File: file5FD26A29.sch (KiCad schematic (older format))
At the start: 4 parts

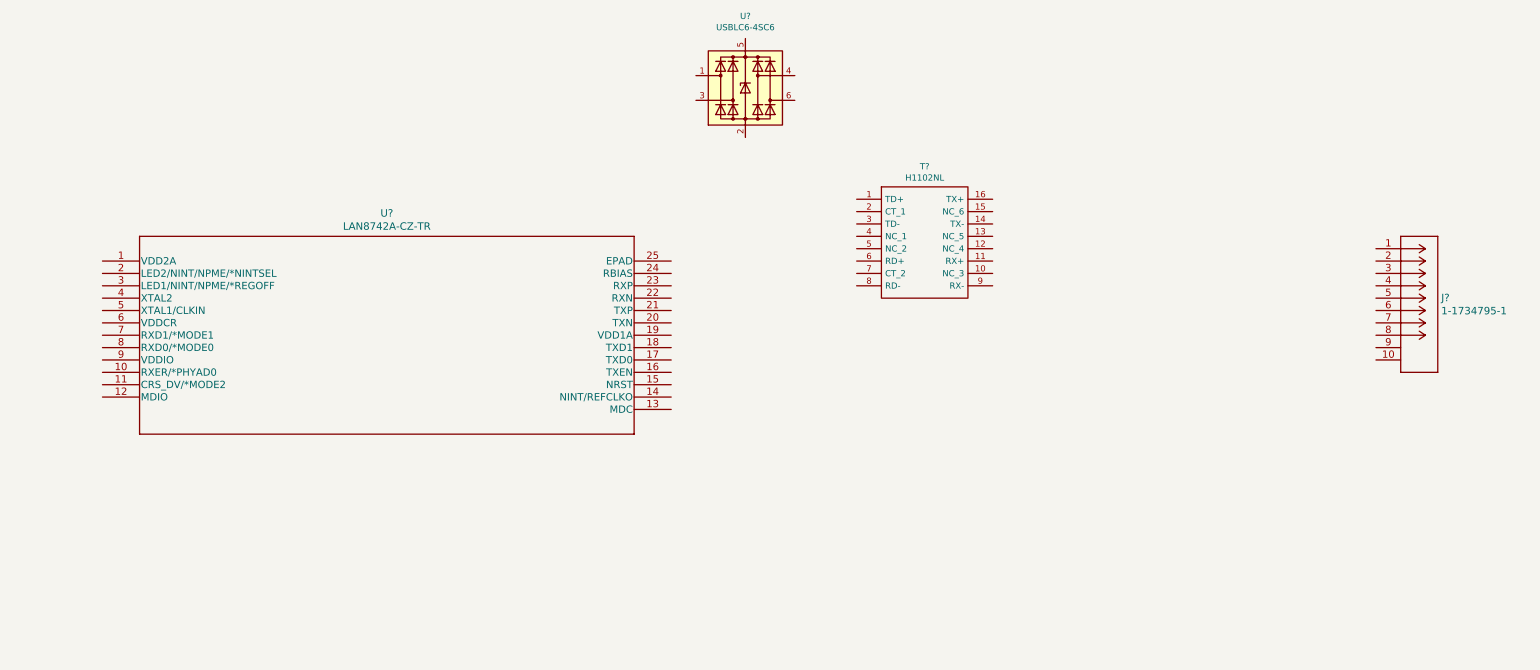
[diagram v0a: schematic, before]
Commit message: Change Ethernet jack
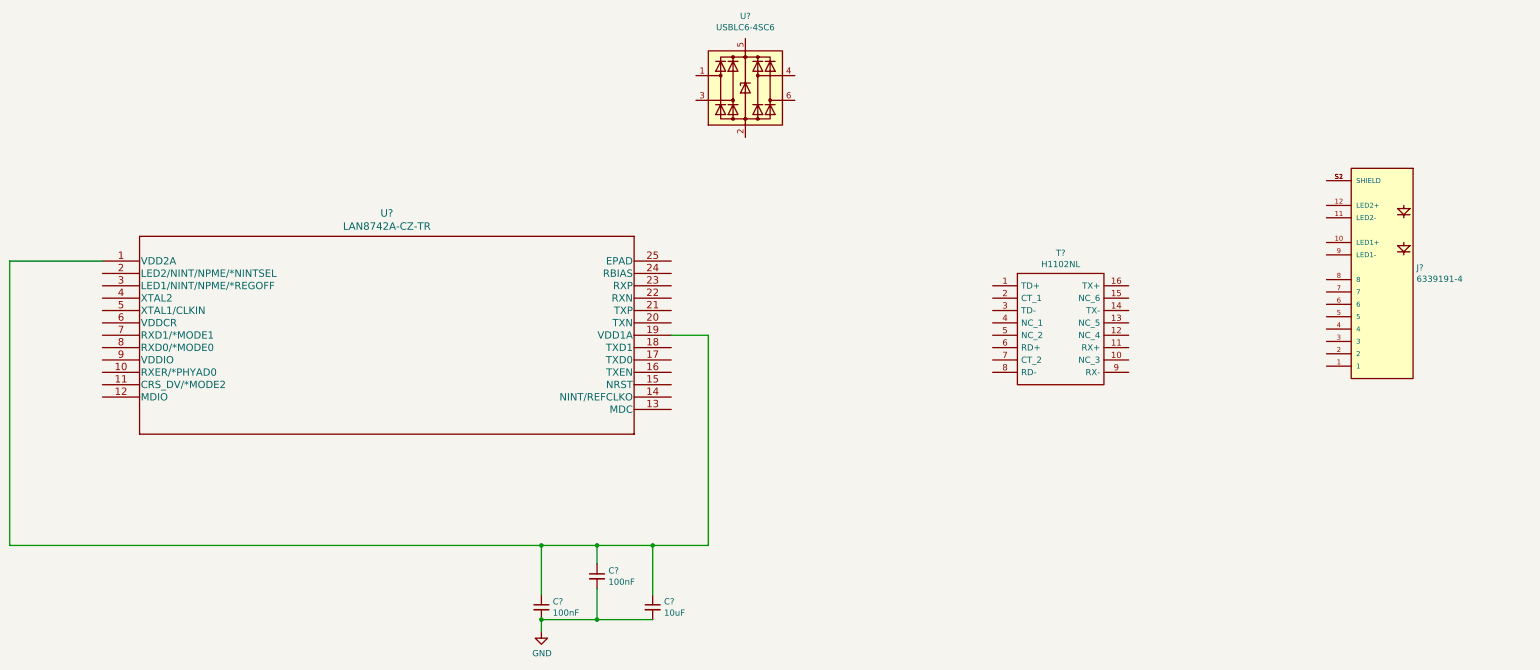
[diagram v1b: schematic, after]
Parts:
- removed J?: 1-1734795-1, CONN12_1-1734795-1_TEC, symbol 2020-12-10_19-10-13:1-1734795-1
- added C? (x2): 100nF, symbol Device:C_Small
- added C?: 10uF, symbol Device:C_Small
- added J?: 6339191-4, TE_6339191-4, symbol 6339191-4:6339191-4
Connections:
- net at U?.1 (VDD2A): now also U?.19 (VDD1A), C?.1, C?.1, C?.1
- new net: J?.S1 (SHIELD), J?.S2 (SHIELD)
- new net GND: C?.2, C?.2, C?.2
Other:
- moved on the sheet: T?
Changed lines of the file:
@@
 L H1102NL:H1102NL T?
 U 1 1 5FD29DFA
-P 8750 4550
-F 0 "T?" H 9300 4815 50  0000 C CNN
-F 1 "H1102NL" H 9300 4724 50  0000 C CNN
-F 2 "SOIC127P940X597-16N" H 9700 4650 50  0001 L CNN
-F 3 "https://productfinder.pulseeng.com/products/datasheets/h1102nl.pdf" H 9700 4550 50  0001 L CNN
-F 4 "PULSE ELECTRONICS - H1102NL - TRANSFORMER, 1:1, 1PORT, 100BASE-TX, SMT" H 9700 4450 50  0001 L CNN "Description"
-F 5 "5.97" H 9700 4350 50  0001 L CNN "Height"
-F 6 "Pulse" H 9700 4250 50  0001 L CNN "Manufacturer_Name"
-F 7 "H1102NL" H 9700 4150 50  0001 L CNN "Manufacturer_Part_Number"
-F 8 "H1102NL" H 9700 4050 50  0001 L CNN "Arrow Part Number"
-F 9 "https://www.arrow.com/en/products/h1102nl/pulse-electronics-corporation" H 9700 3950 50  0001 L CNN "Arrow Price/Stock"
-F 10 "673-H1102NL" H 9700 3850 50  0001 L CNN "Mouser Part Number"
-F 11 "https://www.mouser.co.uk/ProductDetail/Pulse-Electronics/H1102NL?qs=EKu32SdDin%2FHU33L94JZxw%3D%3D" H 9700 3750 50  0001 L CNN "Mouser Price/Stock"
-	1    8750 4550
+P 9850 5250
+F 0 "T?" H 10400 5515 50  0000 C CNN
+F 1 "H1102NL" H 10400 5424 50  0000 C CNN
+F 2 "SOIC127P940X597-16N" H 10800 5350 50  0001 L CNN
+F 3 "https://productfinder.pulseeng.com/products/datasheets/h1102nl.pdf" H 10800 5250 50  0001 L CNN
+F 4 "PULSE ELECTRONICS - H1102NL - TRANSFORMER, 1:1, 1PORT, 100BASE-TX, SMT" H 10800 5150 50  0001 L CNN "Description"
+F 5 "5.97" H 10800 5050 50  0001 L CNN "Height"
+F 6 "Pulse" H 10800 4950 50  0001 L CNN "Manufacturer_Name"
+F 7 "H1102NL" H 10800 4850 50  0001 L CNN "Manufacturer_Part_Number"
+F 8 "H1102NL" H 10800 4750 50  0001 L CNN "Arrow Part Number"
+F 9 "https://www.arrow.com/en/products/h1102nl/pulse-electronics-corporation" H 10800 4650 50  0001 L CNN "Arrow Price/Stock"
+F 10 "673-H1102NL" H 10800 4550 50  0001 L CNN "Mouser Part Number"
+F 11 "https://www.mouser.co.uk/ProductDetail/Pulse-Electronics/H1102NL?qs=EKu32SdDin%2FHU33L94JZxw%3D%3D" H 10800 4450 50  0001 L CNN "Mouser Price/Stock"
+	1    9850 5250
 	1    0    0    -1
 $EndComp
 $Comp
-L 2020-12-10_19-10-13:1-1734795-1 J?
-U 1 1 5FD30F50
-P 12950 4950
-F 0 "J?" H 13478 4553 60  0000 L CNN
-F 1 "1-1734795-1" H 13478 4447 60  0000 L CNN
-F 2 "CONN12_1-1734795-1_TEC" H 13350 4090 60  0001 C CNN
-F 3 "" H 12950 4950 60  0000 C CNN
-	1    12950 4950
+L Device:C_Small C?
+U 1 1 5FD32DB4
+P 6200 7850
+F 0 "C?" H 6292 7896 50  0000 L CNN
+F 1 "100nF" H 6292 7805 50  0000 L CNN
+F 2 "" H 6200 7850 50  0001 C CNN
+F 3 "~" H 6200 7850 50  0001 C CNN
+	1    6200 7850
 	1    0    0    -1
 $EndComp
+$Comp
+L Device:C_Small C?
+U 1 1 5FD339FE
+P 6650 7600
+F 0 "C?" H 6742 7646 50  0000 L CNN
+F 1 "100nF" H 6742 7555 50  0000 L CNN
+F 2 "" H 6650 7600 50  0001 C CNN
+F 3 "~" H 6650 7600 50  0001 C CNN
+	1    6650 7600
+	1    0    0    -1
+$EndComp
+$Comp
+L Device:C_Small C?
+U 1 1 5FD33C45
+P 7100 7850
+F 0 "C?" H 7192 7896 50  0000 L CNN
+F 1 "10uF" H 7192 7805 50  0000 L CNN
+F 2 "" H 7100 7850 50  0001 C CNN
+F 3 "~" H 7100 7850 50  0001 C CNN
+	1    7100 7850
+	1    0    0    -1
+$EndComp
+Wire Wire Line
+	7250 5650 7550 5650
+Wire Wire Line
+	7550 5650 7550 7350
+Wire Wire Line
+	7550 7350 7100 7350
+Wire Wire Line
+	6200 7750 6200 7350
+Wire Wire Line
+	6650 7500 6650 7350
+Connection ~ 6650 7350
+Wire Wire Line
+	6650 7350 6200 7350
+Wire Wire Line
+	7100 7750 7100 7350
+Connection ~ 7100 7350
+Wire Wire Line
+	7100 7350 6650 7350
+Wire Wire Line
+	2650 5050 1900 5050
+Wire Wire Line
+	1900 5050 1900 7350
+Wire Wire Line
+	6200 7350 1900 7350
+Connection ~ 6200 7350
+Wire Wire Line
+	7100 7950 6650 7950
+Wire Wire Line
+	6650 7700 6650 7950
+Connection ~ 6650 7950
+Wire Wire Line
+	6650 7950 6200 7950
+$Comp
+L power:GND #PWR?
+U 1 1 5FD36E57
+P 6200 8050
+F 0 "#PWR?" H 6200 7800 50  0001 C CNN
+F 1 "GND" H 6205 7877 50  0000 C CNN
+F 2 "" H 6200 8050 50  0001 C CNN
+F 3 "" H 6200 8050 50  0001 C CNN
+	1    6200 8050
+	1    0    0    -1
+$EndComp
+Wire Wire Line
+	6200 8050 6200 7950
+Connection ~ 6200 7950
+$Comp
+L 6339191-4:6339191-4 J?
+U 1 1 5FD3947F
+P 13050 5200
+F 0 "J?" H 12822 5104 50  0000 R CNN
+F 1 "6339191-4" H 12822 5195 50  0000 R CNN
+F 2 "TE_6339191-4" H 13050 5200 50  0001 L BNN
+F 3 "" H 13050 5200 50  0001 L BNN
+F 4 "E3" H 13050 5200 50  0001 L BNN "PARTREV"
+F 5 "TE Connectivity" H 13050 5200 50  0001 L BNN "MANUFACTURER"
+F 6 "Manufacturer Recommendation" H 13050 5200 50  0001 L BNN "STANDARD"
+	1    13050 5200
+	-1   0    0    1
+$EndComp
 $EndSCHEMATC

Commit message: Change PS to SMPS 5v, LDO 3.3V
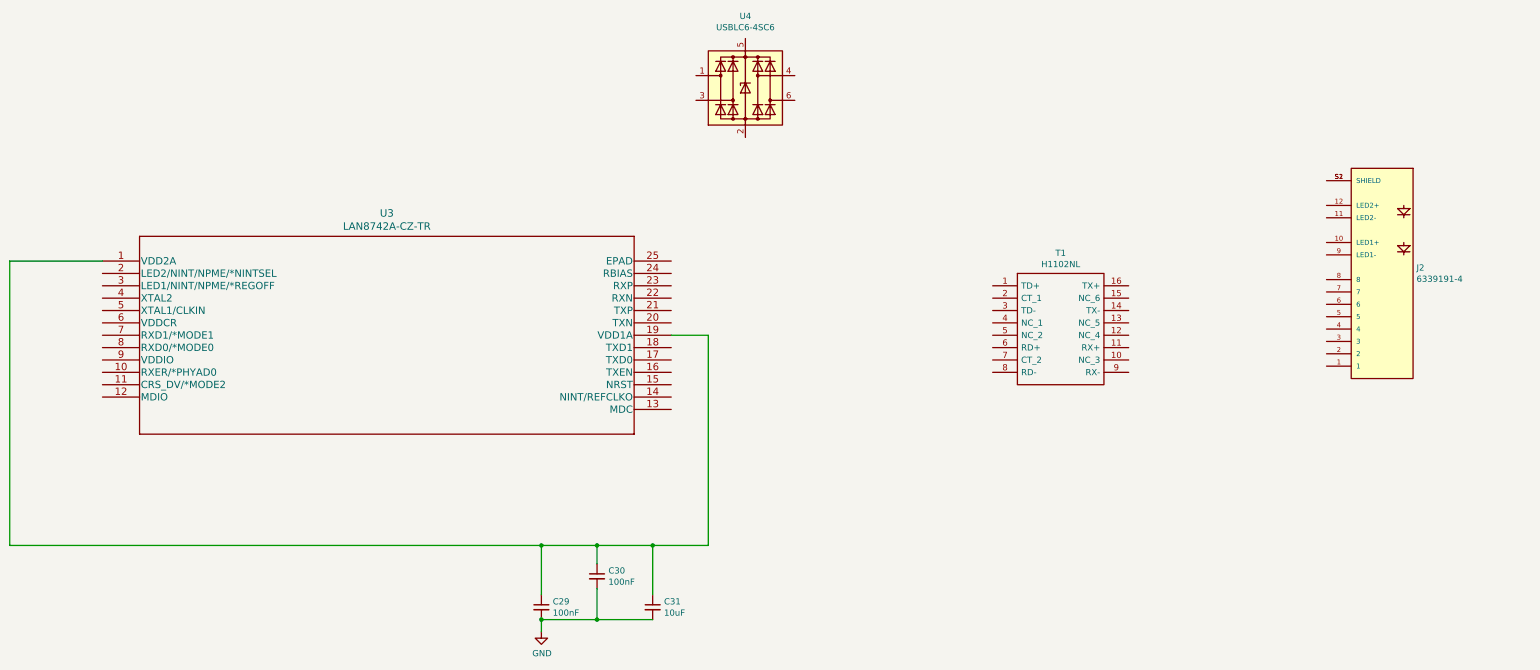
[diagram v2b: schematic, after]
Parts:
- gave numbers to parts that had none: 7
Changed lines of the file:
@@
 $Descr USLedger 17000 11000
 encoding utf-8
-Sheet 5 5
+Sheet 5 6
 Title "KQ9P Power Controller 12VDC"
 Date "2020-12-08"
@@
 $EndDescr
 $Comp
-L 2020-12-10_18-38-26:LAN8742A-CZ-TR U?
+L 2020-12-10_18-38-26:LAN8742A-CZ-TR U3
 U 1 1 5FD274C1
 P 2650 5050
-F 0 "U?" H 4950 5437 60  0000 C CNN
+F 0 "U3" H 4950 5437 60  0000 C CNN
 F 1 "LAN8742A-CZ-TR" H 4950 5331 60  0000 C CNN
 F 2 "SQFN24_4X4MC_MCH" H 4950 5290 60  0001 C CNN
@@
 $EndComp
 $Comp
-L Power_Protection:USBLC6-4SC6 U?
+L Power_Protection:USBLC6-4SC6 U4
 U 1 1 5FD2935E
 P 7850 3650
-F 0 "U?" H 7850 4231 50  0000 C CNN
+F 0 "U4" H 7850 4231 50  0000 C CNN
 F 1 "USBLC6-4SC6" H 7850 4140 50  0000 C CNN
 F 2 "Package_TO_SOT_SMD:SOT-23-6" H 7850 3150 50  0001 C CNN
@@
 $EndComp
 $Comp
-L H1102NL:H1102NL T?
+L H1102NL:H1102NL T1
 U 1 1 5FD29DFA
 P 9850 5250
-F 0 "T?" H 10400 5515 50  0000 C CNN
+F 0 "T1" H 10400 5515 50  0000 C CNN
 F 1 "H1102NL" H 10400 5424 50  0000 C CNN
 F 2 "SOIC127P940X597-16N" H 10800 5350 50  0001 L CNN
@@
 $EndComp
 $Comp
-L Device:C_Small C?
+L Device:C_Small C29
 U 1 1 5FD32DB4
 P 6200 7850
-F 0 "C?" H 6292 7896 50  0000 L CNN
+F 0 "C29" H 6292 7896 50  0000 L CNN
 F 1 "100nF" H 6292 7805 50  0000 L CNN
 F 2 "" H 6200 7850 50  0001 C CNN
@@
 $EndComp
 $Comp
-L Device:C_Small C?
+L Device:C_Small C30
 U 1 1 5FD339FE
 P 6650 7600
-F 0 "C?" H 6742 7646 50  0000 L CNN
+F 0 "C30" H 6742 7646 50  0000 L CNN
 F 1 "100nF" H 6742 7555 50  0000 L CNN
 F 2 "" H 6650 7600 50  0001 C CNN
@@
 $EndComp
 $Comp
-L Device:C_Small C?
+L Device:C_Small C31
 U 1 1 5FD33C45
 P 7100 7850
-F 0 "C?" H 7192 7896 50  0000 L CNN
+F 0 "C31" H 7192 7896 50  0000 L CNN
 F 1 "10uF" H 7192 7805 50  0000 L CNN
 F 2 "" H 7100 7850 50  0001 C CNN
@@
 	6650 7950 6200 7950
 $Comp
-L power:GND #PWR?
+L power:GND #PWR08
 U 1 1 5FD36E57
 P 6200 8050
-F 0 "#PWR?" H 6200 7800 50  0001 C CNN
+F 0 "#PWR08" H 6200 7800 50  0001 C CNN
 F 1 "GND" H 6205 7877 50  0000 C CNN
 F 2 "" H 6200 8050 50  0001 C CNN
@@
 Connection ~ 6200 7950
 $Comp
-L 6339191-4:6339191-4 J?
+L 6339191-4:6339191-4 J2
 U 1 1 5FD3947F
 P 13050 5200
-F 0 "J?" H 12822 5104 50  0000 R CNN
+F 0 "J2" H 12822 5104 50  0000 R CNN
 F 1 "6339191-4" H 12822 5195 50  0000 R CNN
 F 2 "TE_6339191-4" H 13050 5200 50  0001 L BNN
